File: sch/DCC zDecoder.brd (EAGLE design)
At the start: 100 x 80 mm, 24 parts, among them IC1 5V, IC2 ULN2803, IC3 ULN2803, X10 22-23-2031, X11 22-23-2031, X12 22-23-2031, X7 22-23-2031, X8 22-23-2031, X9 22-23-2031

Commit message: added values
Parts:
- C1: value (none) -> 2200u 35V
- R1: value (none) -> 4.7k
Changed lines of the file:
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@@
 <attribute name="VALUE" x="84.2518" y="55.2196" size="1.27" layer="27" ratio="10"/>
 </element>
-<element name="C1" library="rcl" library_urn="urn:adsk.eagle:library:334" package="E5-8,5" package3d_urn="urn:adsk.eagle:package:23374/1" value="" x="74.93" y="55.88" smashed="yes" rot="R270">
+<element name="C1" library="rcl" library_urn="urn:adsk.eagle:library:334" package="E5-8,5" package3d_urn="urn:adsk.eagle:package:23374/1" value="2200u 35V" x="74.93" y="55.88" smashed="yes" rot="R270">
 <attribute name="NAME" x="77.216" y="51.7398" size="1.27" layer="25" ratio="10" rot="R270"/>
 <attribute name="POPULARITY" value="0" x="-22.86" y="12.7" size="1.778" layer="27" rot="R270" display="off"/>
@@
 <attribute name="VALUE" x="48.895" y="73.406" size="1.27" layer="27" ratio="10" rot="R270"/>
 </element>
-<element name="R1" library="rcl" library_urn="urn:adsk.eagle:library:334" package="0207/10" package3d_urn="urn:adsk.eagle:package:23491/2" value="" x="76.2" y="63.5" smashed="yes">
+<element name="R1" library="rcl" library_urn="urn:adsk.eagle:library:334" package="0207/10" package3d_urn="urn:adsk.eagle:package:23491/2" value="4.7k" x="76.2" y="63.5" smashed="yes">
 <attribute name="NAME" x="73.152" y="65.024" size="1.27" layer="25" ratio="10"/>
 <attribute name="POPULARITY" value="81" x="130.81" y="-31.75" size="1.778" layer="27" display="off"/>

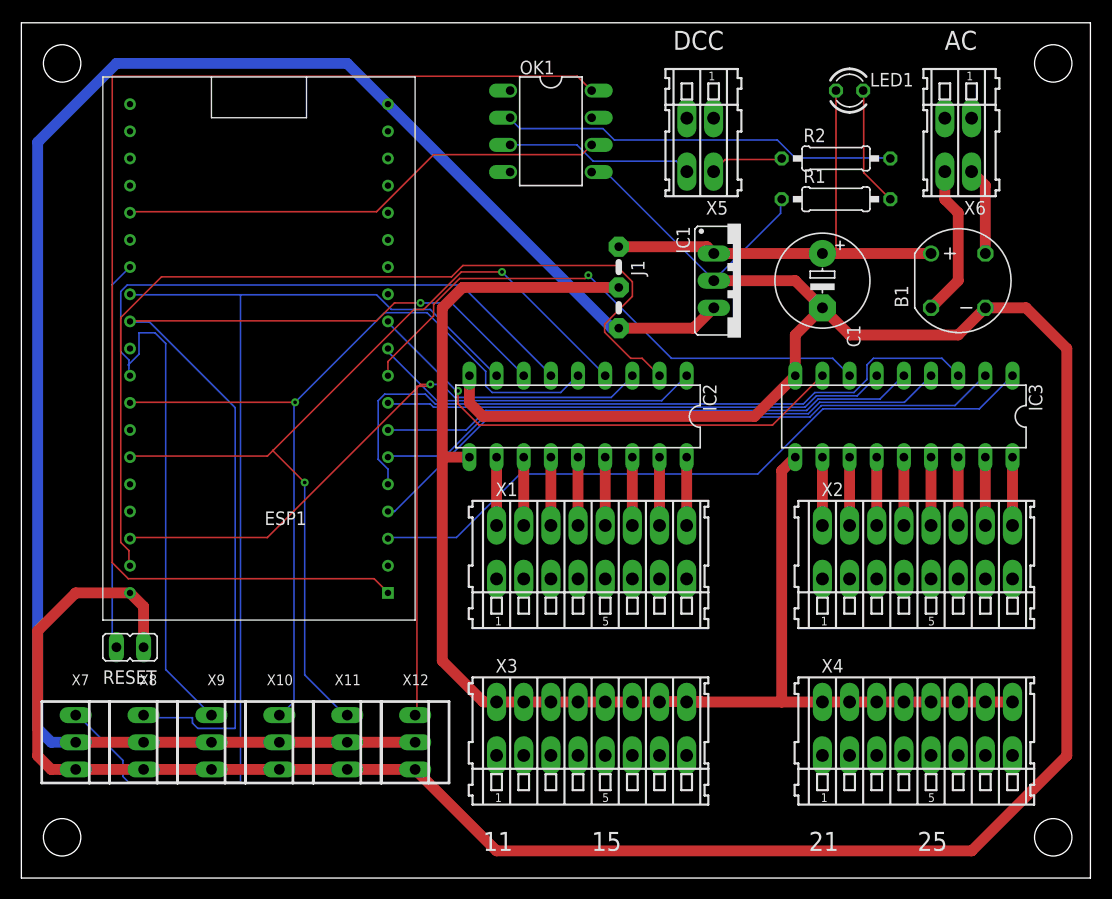
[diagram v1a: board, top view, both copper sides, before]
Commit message: reset pin added and pin mapping changed
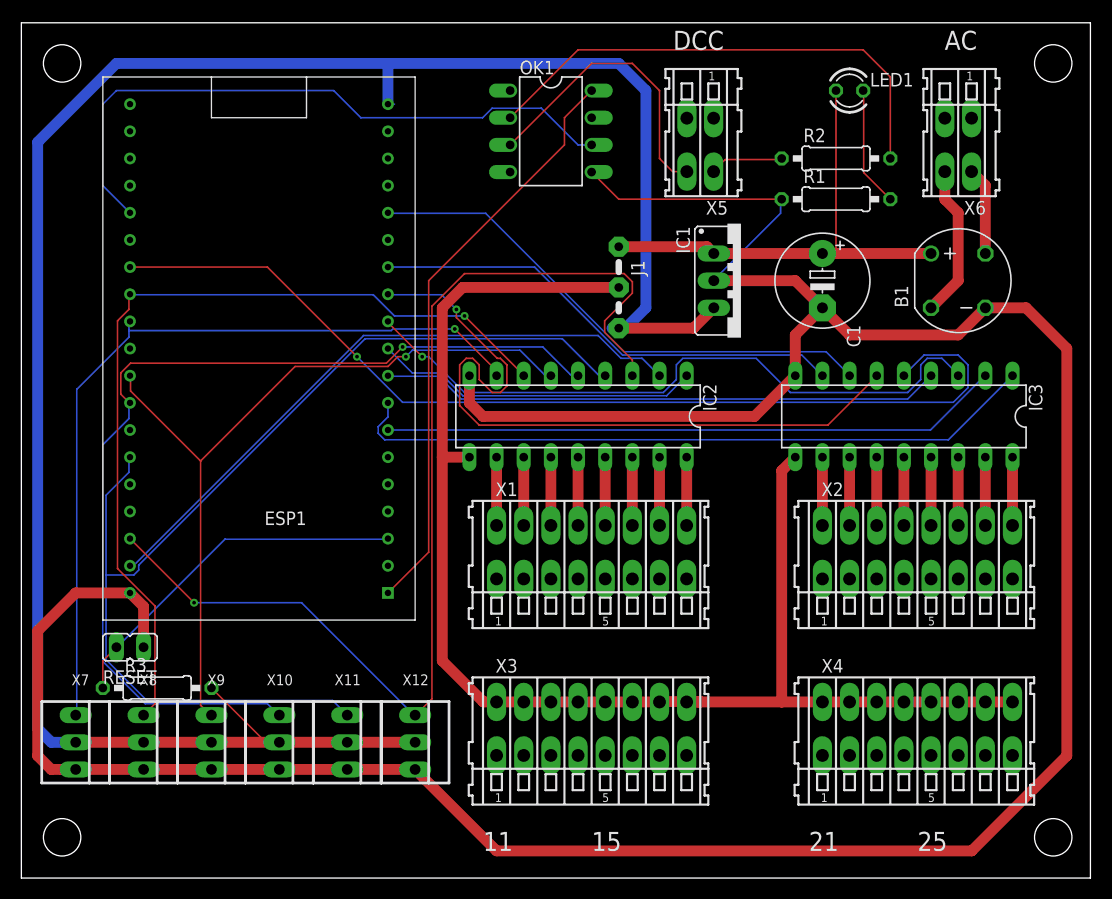
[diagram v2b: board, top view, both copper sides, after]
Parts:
- added R3: 10k, rcl:0207/10
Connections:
- removed net N$15: ESP1.26, RESET.1
- removed net TCK: ESP1.15
- removed net TDI: ESP1.13
- removed net TDO: ESP1.23
- removed net TMS: ESP1.12
- new net GPIO39: ESP1.3, R3.1, RESET.1
- net +5V: now also R3.2
- net O11: now also ESP1.28; no longer ESP1.27
- net O12: now also ESP1.27; no longer ESP1.28
- net O21: now also ESP1.13; no longer ESP1.11
- net O22: now also ESP1.15; no longer ESP1.9
- net O23: now also ESP1.12; no longer ESP1.8
- net O24: now also ESP1.26; no longer ESP1.7
- net O25: now also ESP1.9; no longer ESP1.6
- net O26: now also ESP1.11; no longer ESP1.5
- net O27: now also ESP1.7; no longer ESP1.4
- net O28: now also ESP1.8; no longer ESP1.3
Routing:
- net +3V3: track 117.9 -> 54.9 mm
- net O24: track 50.4 -> 93.5 mm, vias 0 -> 1
- net N$15: track 36.5 -> 0.00 mm
- net GPIO39: track 0.00 -> 34.0 mm
- net +5V: track 168.8 -> 198.7 mm
- net O17: track 86.7 -> 60.0 mm
- net O11: track 101.9 -> 75.5 mm, vias 0 -> 1
- net O13: track 95.2 -> 73.1 mm, vias 0 -> 1
- net O23: track 47.2 -> 68.9 mm, vias 0 -> 1
- net O15: track 83.4 -> 102.2 mm, vias 2 -> 0
- net O16: track 86.5 -> 103.7 mm
- net GPIO2: track 45.8 -> 60.3 mm
- net O14: track 79.9 -> 91.9 mm
- net O12: track 93.0 -> 81.8 mm
- net N$11: track 17.6 -> 27.6 mm
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
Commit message: partlist updated
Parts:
- B1: value (none) -> B80R DIO
- ESP1: value (none) -> ESP32 NodeMCU
- IC1: value 5V -> TSR 1-2450
- J1: value (none) -> MPE 087-1-003
- LED1: value green -> green 3mm
- RESET: value (none) -> MPE 087-1-002
- X1, X2, X3, X4: value (none) -> DG240 2,54-8
- X10, X11, X12, X7, X8, X9: value 22-23-2031 -> PSS 254/3G
- X5, X6: value (none) -> DG240 2,54-2

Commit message: backup
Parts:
- added F1: 900mA, fuse:TE5
- ESP1: value ESP32 NodeMCU -> NodeMCU CH340C; device _esp32:ESP32_NODEMCU -> _esp32:ESP32_NODEMCU_CH340C
- moved ESP1 25.7 mm to (8.89, 63.5)
- moved R3 24.7 mm to (4.32, 41.0), turned to 90 degrees
- moved RESET 11.5 mm to (4.32, 31.5), turned to 180 degrees
- moved R1 1.27 mm to (76.2, 64.8)
- moved R2 1.27 mm to (76.2, 68.6)
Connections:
- removed net GND1: ESP1.14
- removed net GND2: ESP1.32
- new net N$15: F1.1, X6.A1
- net +3V3: now also ESP1.P$1; no longer ESP1.1
- net +5V: now also ESP1.P$30; no longer ESP1.19
- net GND: now also ESP1.P$2, ESP1.P$29; no longer ESP1.38
- net GPIO2: now also ESP1.P$4; no longer ESP1.24
- net GPIO39: now also ESP1.P$18; no longer ESP1.3
- net N$5: now also F1.2; no longer X6.A1
- net O11: now also ESP1.P$15; no longer ESP1.28
- net O12: now also ESP1.P$14; no longer ESP1.27
- net O13: now also ESP1.P$11; no longer ESP1.30
- net O14: now also ESP1.P$10; no longer ESP1.31
- net O15: now also ESP1.P$9; no longer ESP1.33
- net O16: now also ESP1.P$7; no longer ESP1.36
- net O17: now also ESP1.P$6; no longer ESP1.37
- net O18: now also ESP1.P$5; no longer ESP1.10
- net O21: now also ESP1.P$21; no longer ESP1.13
- net O22: now also ESP1.P$22; no longer ESP1.15
- net O23: now also ESP1.P$23; no longer ESP1.12
- net O24: now also ESP1.P$24; no longer ESP1.26
- net O25: now also ESP1.P$25; no longer ESP1.9
- net O26: now also ESP1.P$26; no longer ESP1.11
- net O27: now also ESP1.P$27; no longer ESP1.7
- net O28: now also ESP1.P$28; no longer ESP1.8
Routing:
- net O24: track 93.5 -> 50.4 mm, vias 1 -> 0
- net GND: track 280.7 -> 240.6 mm
- net O18: track 30.5 -> 67.7 mm
- net O23: track 68.9 -> 46.8 mm, vias 1 -> 0
- net O12: track 81.8 -> 62.0 mm
- net O15: track 102.2 -> 86.0 mm
- net O14: track 91.9 -> 80.4 mm
- net GPIO2: track 60.3 -> 49.2 mm
- net N$15: track 0.00 -> 10.8 mm
- net N$11: track 27.6 -> 17.6 mm
- net O27: track 58.0 -> 64.6 mm, vias 0 -> 1
- net O16: track 103.7 -> 97.5 mm, vias 1 -> 0
- net O22: track 49.5 -> 44.5 mm
- net O17: track 60.0 -> 55.0 mm, vias 0 -> 1
- net +3V3: track 54.9 -> 51.9 mm
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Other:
- board text added: "5V"
- board text added: "AC / DC"
- board text added: "Vcc"
- board text added: "zDecoder 2023-11-18 AZ"
- board text removed: "AC"

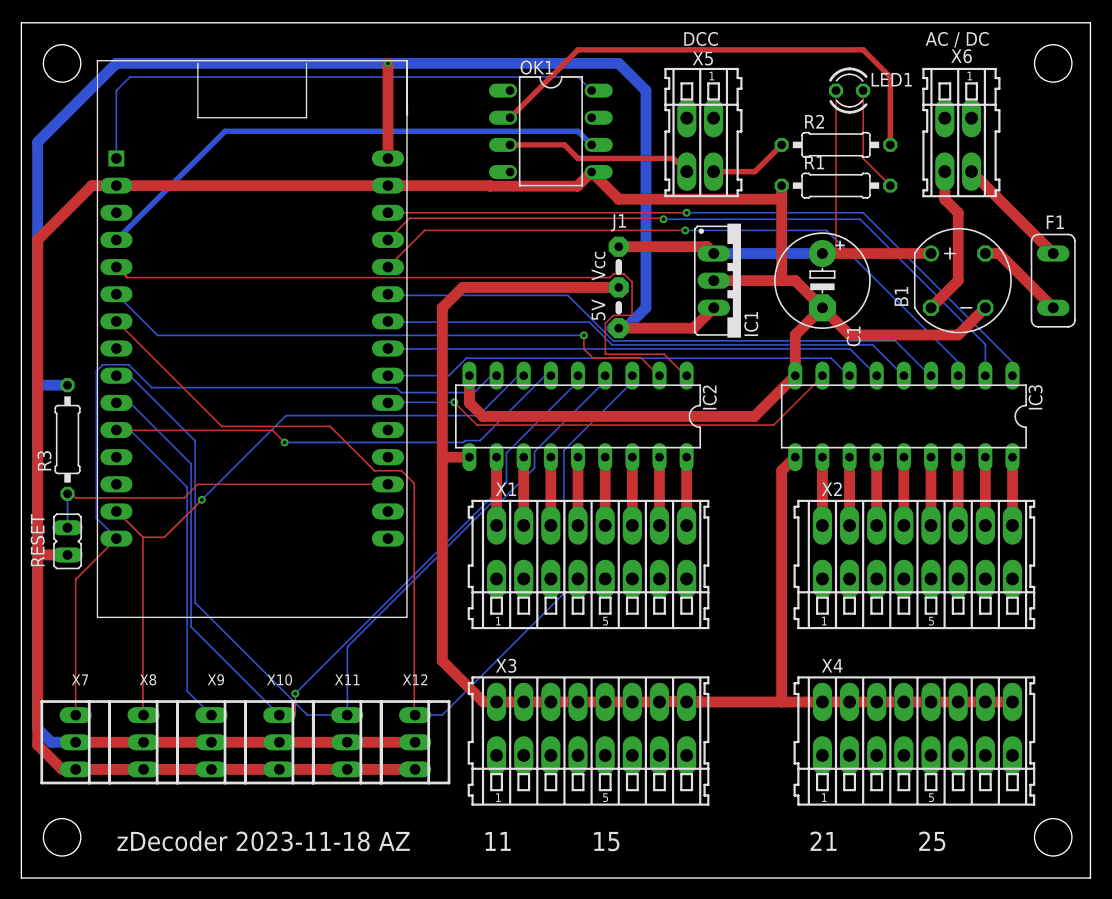
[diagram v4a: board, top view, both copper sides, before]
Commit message: routing changed and fuse added
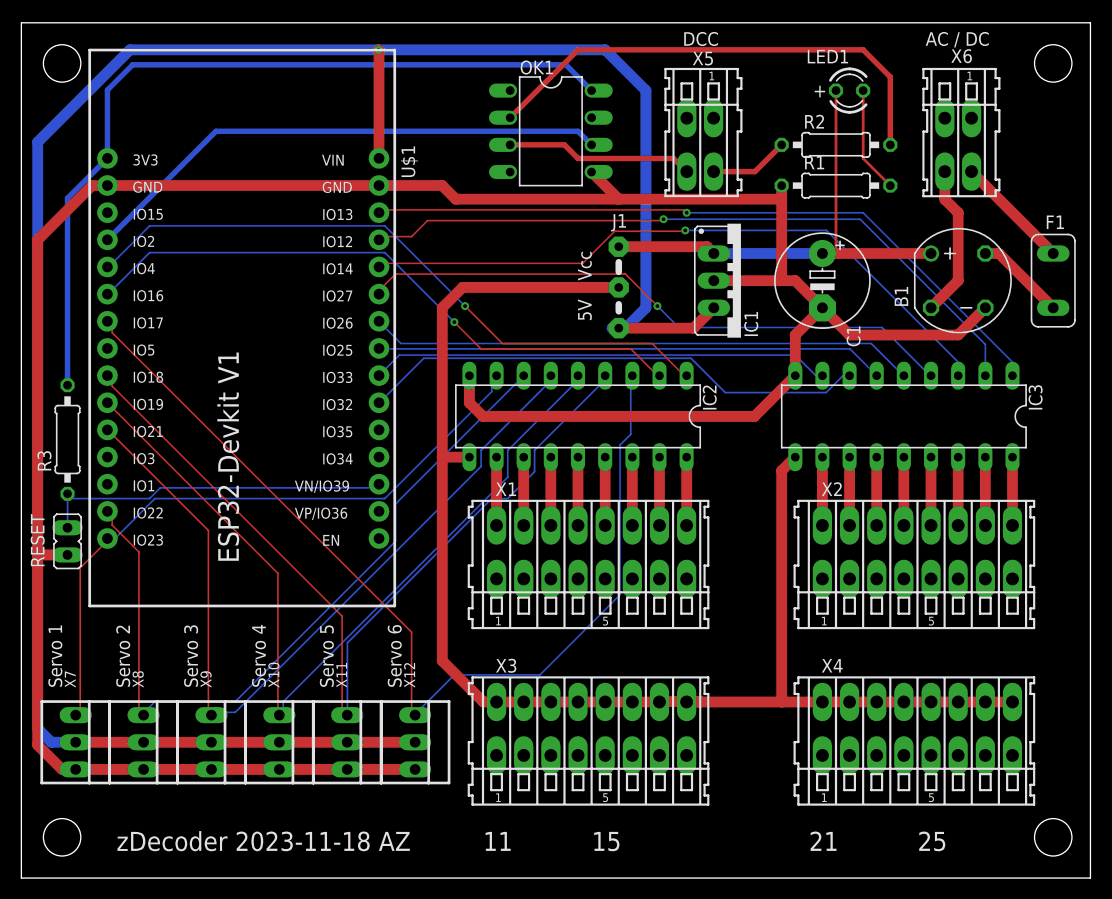
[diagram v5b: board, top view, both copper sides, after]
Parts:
- removed ESP1: NodeMCU CH340C, _esp32:ESP32_NODEMCU_CH340C
- added U$1: ESP32DEVKITV1, _esp32:ESP32-DEVKITV1
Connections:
- net +3V3: now also R3.2, U$1.3V3; no longer ESP1.P$1
- net +5V: now also U$1.VIN; no longer ESP1.P$30, R3.2
- net GND: now also U$1.GND@1, U$1.GND@2; no longer ESP1.P$2, ESP1.P$29
- net GPIO2: now also U$1.D2; no longer ESP1.P$4
- net GPIO39: now also U$1.D39; no longer ESP1.P$18
- net O11: now also U$1.D23; no longer ESP1.P$15
- net O12: now also U$1.D22; no longer ESP1.P$14
- net O13: now also U$1.D21; no longer ESP1.P$11
- net O14: now also U$1.D19; no longer ESP1.P$10
- net O15: now also U$1.D18; no longer ESP1.P$9
- net O16: now also U$1.D17; no longer ESP1.P$7
- net O17: now also U$1.D16; no longer ESP1.P$6
- net O18: now also U$1.D4; no longer ESP1.P$5
- net O21: now also U$1.D33; no longer ESP1.P$21
- net O22: now also U$1.D32; no longer ESP1.P$22
- net O23: now also U$1.D25; no longer ESP1.P$23
- net O24: now also U$1.D26; no longer ESP1.P$24
- net O25: now also U$1.D27; no longer ESP1.P$25
- net O26: now also U$1.D14; no longer ESP1.P$26
- net O27: now also U$1.D12; no longer ESP1.P$27
- net O28: now also U$1.D13; no longer ESP1.P$28
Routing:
- net +3V3: track 51.9 -> 76.4 mm
- net O11: track 73.9 -> 61.3 mm
- net O12: track 62.0 -> 71.4 mm, vias 1 -> 0
- net O18: track 67.7 -> 61.5 mm, vias 0 -> 1
- net O16: track 97.5 -> 93.8 mm
- net O22: track 44.5 -> 47.7 mm
- net O17: track 55.0 -> 58.0 mm
- net O25: track 54.0 -> 56.5 mm, vias 0 -> 1
- net GND: track 240.6 -> 243.1 mm
- net O15: track 86.0 -> 84.0 mm
- net O13: track 75.0 -> 76.8 mm, vias 1 -> 0
- net O14: track 80.4 -> 79.2 mm, vias 1 -> 0
- net O28: track 65.5 -> 66.7 mm
- net O26: track 61.1 -> 62.1 mm
- net O27: track 64.6 -> 65.5 mm
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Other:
- board text added: "+"
- board text added: "Servo 1"
- board text added: "Servo 2"
- board text added: "Servo 3"
- board text added: "Servo 4"
- board text added: "Servo 5"
- board text added: "Servo 6"

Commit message: Version 1.0
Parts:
- added C2: 10u, rcl:C050-024X044
- added C3, C4, C5: 100n, rcl:C050-024X044
- IC1: value TSR 1-2450 -> R-78E05-1.0; device v-reg:78XXS -> _eigene:R-78E-XX1.0
- moved J1 5.08 mm to (50.8, 57.1)
- moved IC1 3.81 mm to (63.5, 55.9)
- renumbered U$1 to ESP1
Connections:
- net +5V: now also C2.1, C3.1, C4.1, C5.1
- net GND: now also C2.2, C3.2, C4.2, C5.2
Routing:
- net GND: track 243.1 -> 260.0 mm
- net +5V: track 198.3 -> 214.6 mm
- net VCC: track 44.7 -> 49.8 mm
- net V+: track 133.8 -> 128.7 mm
- net N$4: track 7.62 -> 6.39 mm
